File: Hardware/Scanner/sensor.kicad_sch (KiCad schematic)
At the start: 23 parts, among them U1 OPA2376xxD, U4 OPA2376xxD

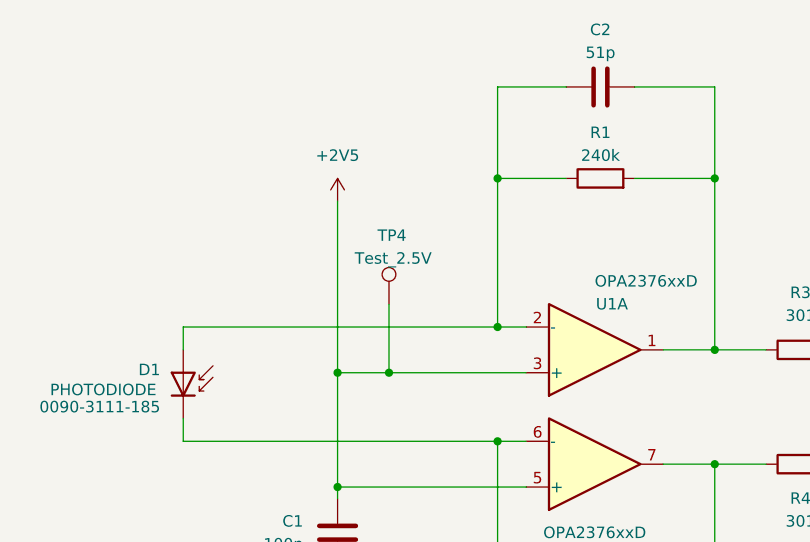
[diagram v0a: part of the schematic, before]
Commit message: Updated LED and crystal descriptions
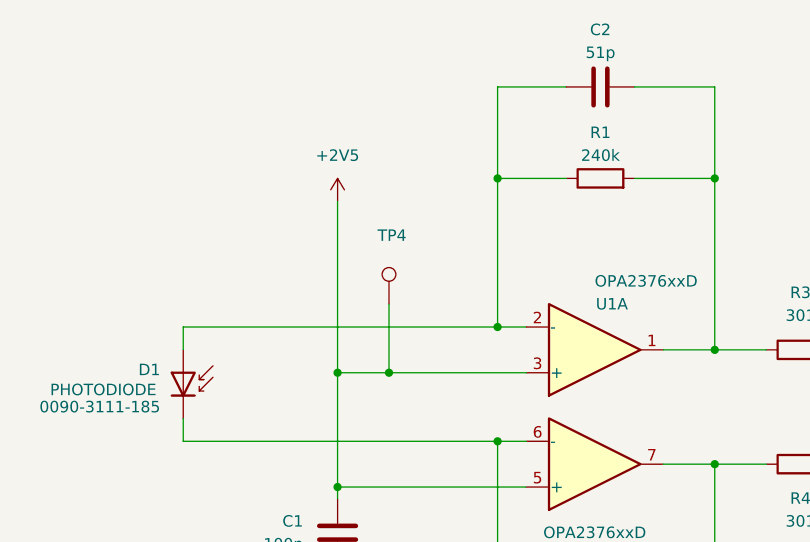
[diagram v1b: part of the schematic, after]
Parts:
- TP4: value Test_2.5V -> (none); footprint TestPoint:TestPoint_Pad_D1.5mm -> (none); now left out of the parts list
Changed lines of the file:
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@@
   )
   (symbol (lib_id "Connector:TestPoint") (at 118.745 46.99 0) (unit 1)
-    (in_bom yes) (on_board yes)
+    (in_bom no) (on_board yes)
     (property "Reference" "TP4" (id 0) (at 117.475 39.37 0)
       (effects (font (size 1.27 1.27)) (justify left))
     )
-    (property "Value" "Test_2.5V" (id 1) (at 114.935 41.91 0)
+    (property "Value" "" (id 1) (at 114.935 41.91 0)
       (effects (font (size 1.27 1.27)) (justify left))
     )
-    (property "Footprint" "TestPoint:TestPoint_Pad_D1.5mm" (id 2) (at 123.825 46.99 0)
+    (property "Footprint" "" (id 2) (at 123.825 46.99 0)
       (effects (font (size 1.27 1.27)) hide)
     )

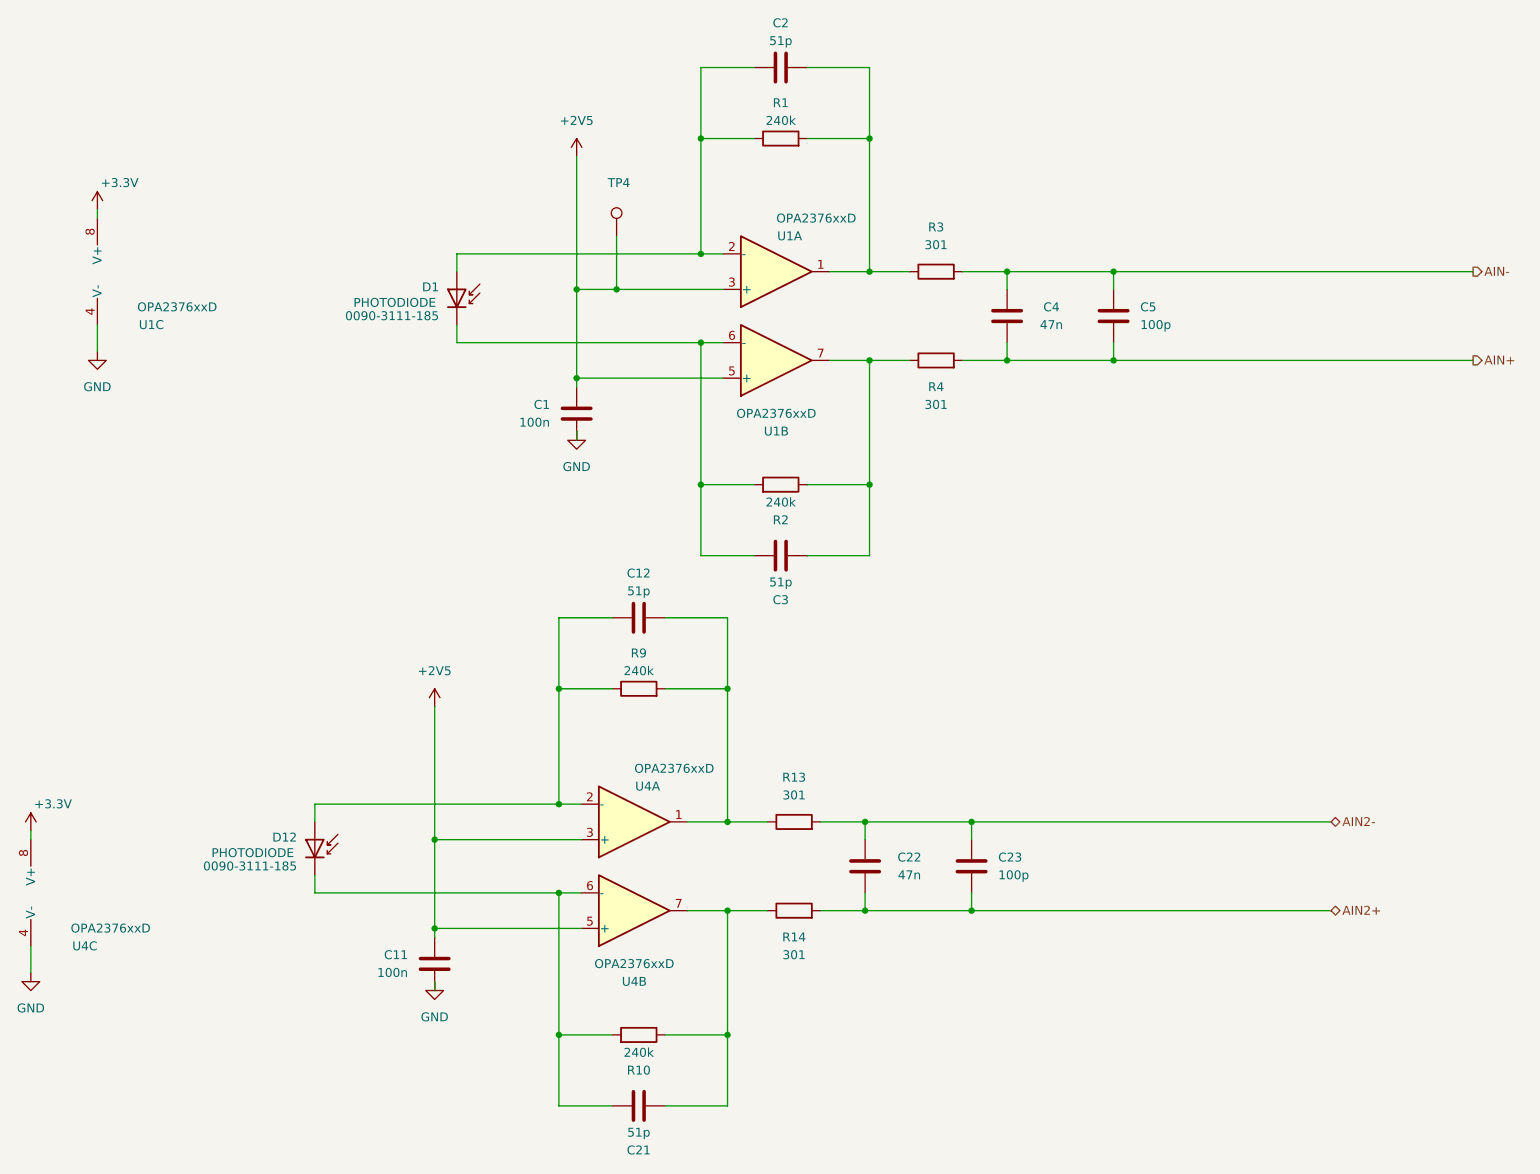
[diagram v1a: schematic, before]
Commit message: Consistency of capacitor values
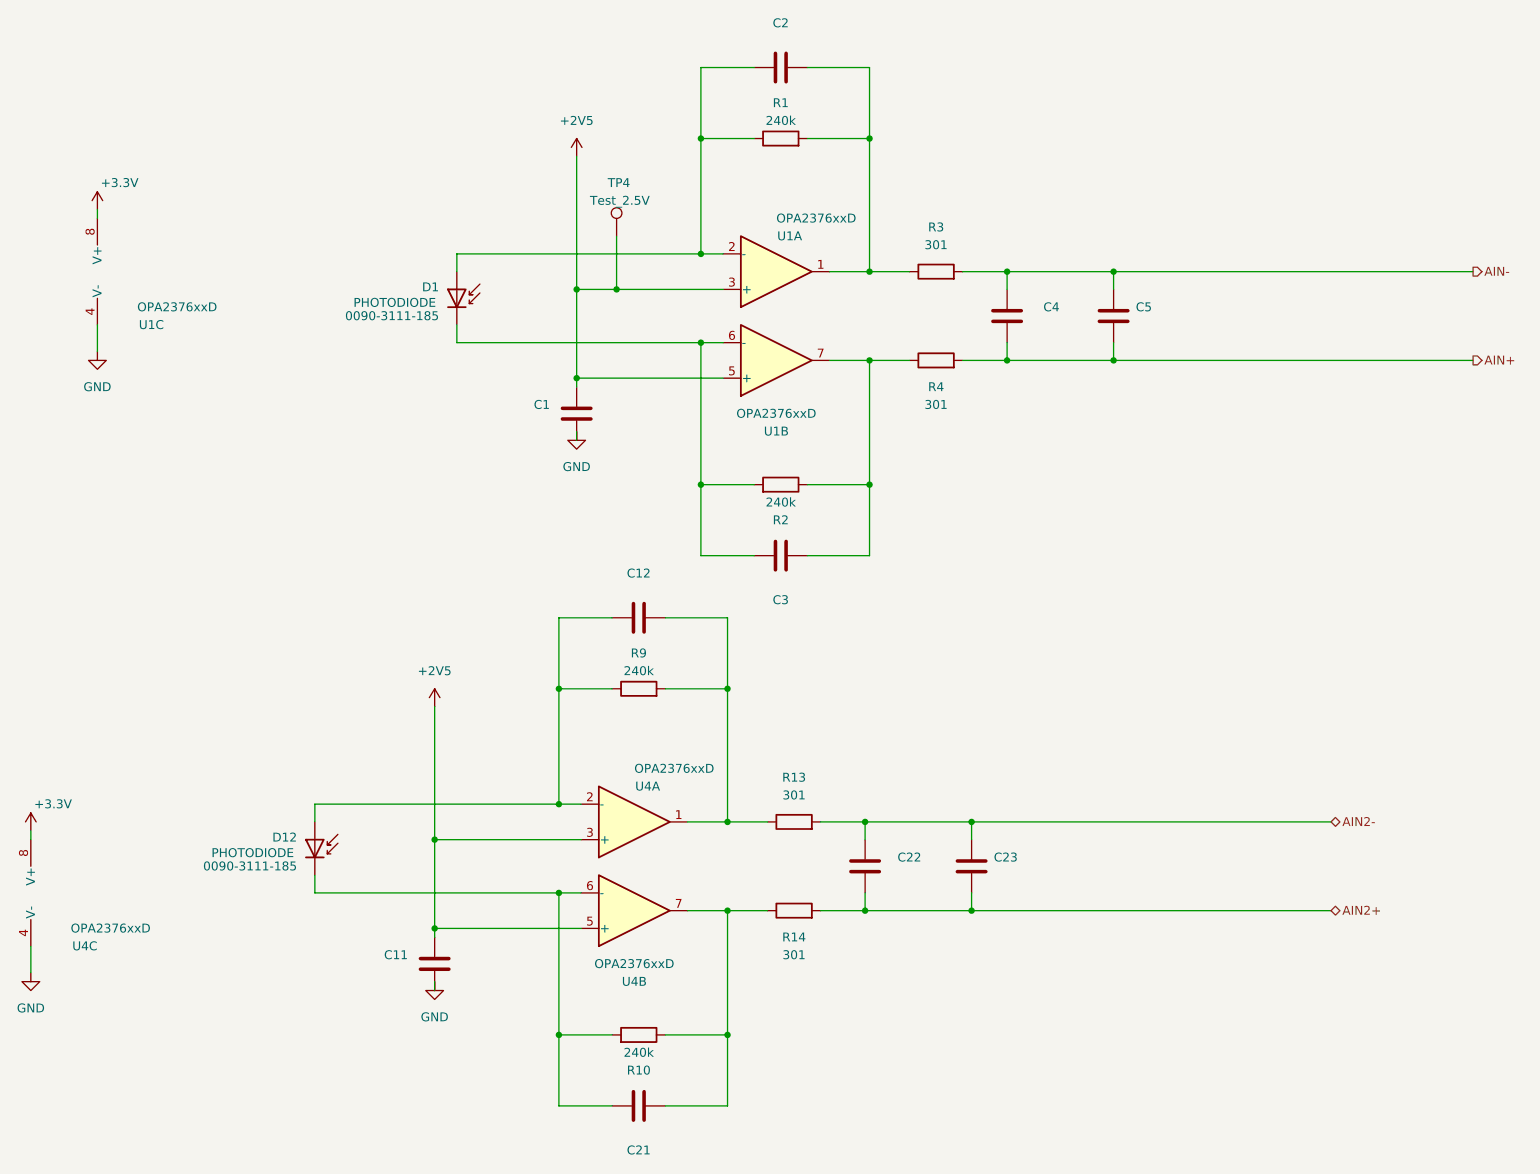
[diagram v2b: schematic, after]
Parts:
- C1, C11: value 100n -> (none)
- C12, C2, C21, C3: value 51p -> (none)
- C22, C4: value 47n -> (none)
- C23, C5: value 100p -> (none)
- TP4: value (none) -> Test_2.5V; footprint (none) -> TestPoint:TestPoint_Pad_D1.5mm
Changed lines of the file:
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@@
       (effects (font (size 1.27 1.27)) (justify right))
     )
-    (property "Value" "100n" (id 1) (at 88.9 152.3999 0)
+    (property "Value" "" (id 1) (at 88.9 152.3999 0)
       (effects (font (size 1.27 1.27)) (justify right))
     )
@@
   (symbol (lib_id "Device:C") (at 189.865 58.42 0) (unit 1)
     (in_bom yes) (on_board yes) (fields_autoplaced)
-    (property "Reference" "C5" (id 0) (at 193.675 57.1499 0)
+    (property "Reference" "C5" (id 0) (at 193.04 57.1499 0)
       (effects (font (size 1.27 1.27)) (justify left))
     )
-    (property "Value" "100p" (id 1) (at 193.675 59.6899 0)
+    (property "Value" "" (id 1) (at 193.04 59.6899 0)
       (effects (font (size 1.27 1.27)) (justify left))
     )
@@
       (effects (font (size 1.27 1.27)) (justify left))
     )
-    (property "Value" "" (id 1) (at 114.935 41.91 0)
+    (property "Value" "Test_2.5V" (id 1) (at 114.935 41.91 0)
       (effects (font (size 1.27 1.27)) (justify left))
     )
-    (property "Footprint" "" (id 2) (at 123.825 46.99 0)
+    (property "Footprint" "TestPoint:TestPoint_Pad_D1.5mm" (id 2) (at 123.825 46.99 0)
       (effects (font (size 1.27 1.27)) hide)
     )
@@
   (symbol (lib_id "Device:C") (at 169.545 137.16 0) (unit 1)
     (in_bom yes) (on_board yes) (fields_autoplaced)
-    (property "Reference" "C23" (id 0) (at 173.355 135.8899 0)
+    (property "Reference" "C23" (id 0) (at 172.72 135.8899 0)
       (effects (font (size 1.27 1.27)) (justify left))
     )
-    (property "Value" "100p" (id 1) (at 173.355 138.4299 0)
+    (property "Value" "" (id 1) (at 172.72 138.4299 0)
       (effects (font (size 1.27 1.27)) (justify left))
     )
@@
     (in_bom yes) (on_board yes)
     (property "Reference" "C12" (id 0) (at 121.92 95.25 90))
-    (property "Value" "51p" (id 1) (at 121.92 97.79 90))
+    (property "Value" "" (id 1) (at 121.92 97.79 90))
     (property "Footprint" "Capacitor_SMD:C_0603_1608Metric_Pad1.08x0.95mm_HandSolder" (id 2) (at 125.73 100.6348 0)
       (effects (font (size 1.27 1.27)) hide)
@@
     (in_bom yes) (on_board yes)
     (property "Reference" "C3" (id 0) (at 142.24 99.06 90))
-    (property "Value" "51p" (id 1) (at 142.24 96.52 90))
+    (property "Value" "" (id 1) (at 142.24 96.52 90))
     (property "Footprint" "Capacitor_SMD:C_0603_1608Metric_Pad1.08x0.95mm_HandSolder" (id 2) (at 146.05 91.7448 0)
       (effects (font (size 1.27 1.27)) hide)
@@
     (in_bom yes) (on_board yes)
     (property "Reference" "C2" (id 0) (at 142.24 16.51 90))
-    (property "Value" "51p" (id 1) (at 142.24 19.05 90))
+    (property "Value" "" (id 1) (at 142.24 19.05 90))
     (property "Footprint" "Capacitor_SMD:C_0603_1608Metric_Pad1.08x0.95mm_HandSolder" (id 2) (at 146.05 21.8948 0)
       (effects (font (size 1.27 1.27)) hide)
@@
     (in_bom yes) (on_board yes)
     (property "Reference" "C4" (id 0) (at 180.975 57.15 0))
-    (property "Value" "47n" (id 1) (at 180.975 59.69 0))
+    (property "Value" "" (id 1) (at 180.975 59.69 0))
     (property "Footprint" "Capacitor_SMD:C_0603_1608Metric_Pad1.08x0.95mm_HandSolder" (id 2) (at 173.6598 54.61 0)
       (effects (font (size 1.27 1.27)) hide)
@@
     (in_bom yes) (on_board yes)
     (property "Reference" "C22" (id 0) (at 160.655 135.89 0))
-    (property "Value" "47n" (id 1) (at 160.655 138.43 0))
+    (property "Value" "" (id 1) (at 160.655 138.43 0))
     (property "Footprint" "Capacitor_SMD:C_0603_1608Metric_Pad1.08x0.95mm_HandSolder" (id 2) (at 153.3398 133.35 0)
       (effects (font (size 1.27 1.27)) hide)
@@
     (in_bom yes) (on_board yes)
     (property "Reference" "C21" (id 0) (at 121.92 177.8 90))
-    (property "Value" "51p" (id 1) (at 121.92 175.26 90))
+    (property "Value" "" (id 1) (at 121.92 175.26 90))
     (property "Footprint" "Capacitor_SMD:C_0603_1608Metric_Pad1.08x0.95mm_HandSolder" (id 2) (at 125.73 170.4848 0)
       (effects (font (size 1.27 1.27)) hide)
@@
       (effects (font (size 1.27 1.27)) (justify right))
     )
-    (property "Value" "100n" (id 1) (at 109.22 73.6599 0)
-      (effects (font (size 1.27 1.27)) (justify right))
-    )
+    (property "Value" "" (id 1) (at 109.22 73.6599 0)
+      (effects (font (size 1.27 1.27)) (justify right))
+    )

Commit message: LAtching circuit for controller board + minors
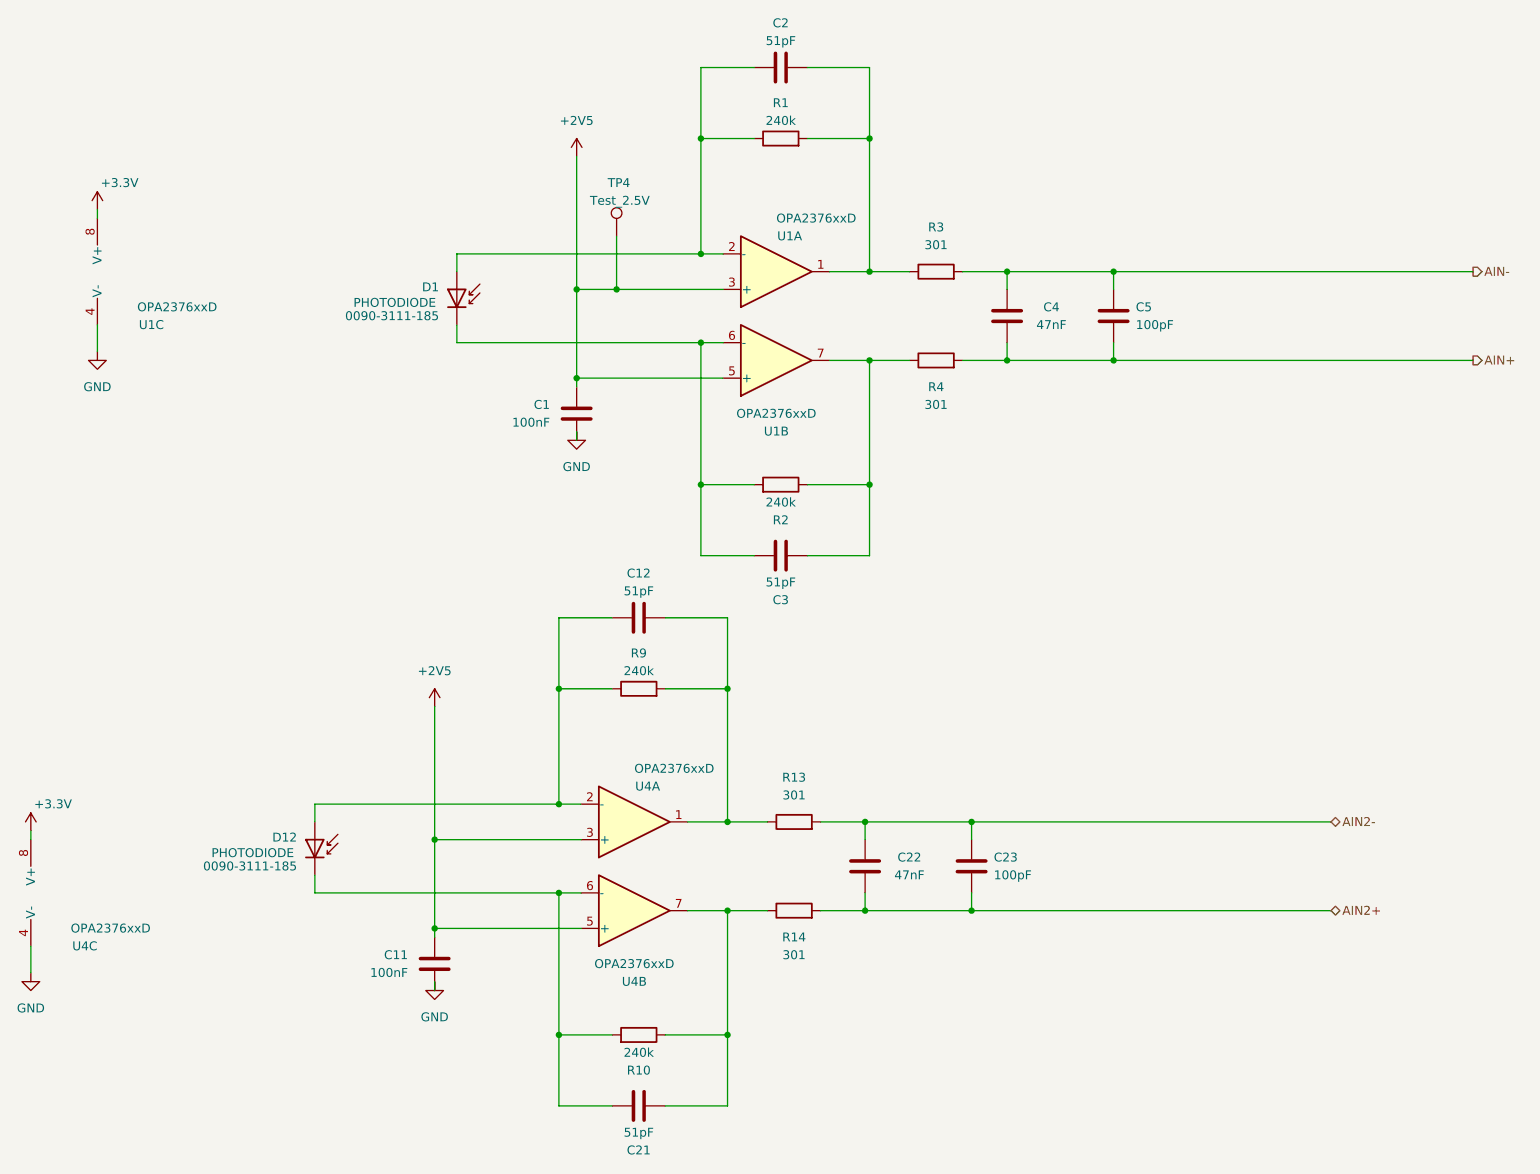
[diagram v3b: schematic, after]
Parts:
- C1, C11: value (none) -> 100nF
- C12, C2, C21, C3: value (none) -> 51pF
- C22, C4: value (none) -> 47nF
- C23, C5: value (none) -> 100pF
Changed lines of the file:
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@@
       (effects (font (size 1.27 1.27)) (justify right))
     )
-    (property "Value" "" (id 1) (at 88.9 152.3999 0)
+    (property "Value" "100nF" (id 1) (at 88.9 152.3999 0)
       (effects (font (size 1.27 1.27)) (justify right))
     )
@@
       (effects (font (size 1.27 1.27)) (justify left))
     )
-    (property "Value" "" (id 1) (at 193.04 59.6899 0)
+    (property "Value" "100pF" (id 1) (at 193.04 59.6899 0)
       (effects (font (size 1.27 1.27)) (justify left))
     )
@@
       (effects (font (size 1.27 1.27)) (justify left))
     )
-    (property "Value" "" (id 1) (at 172.72 138.4299 0)
+    (property "Value" "100pF" (id 1) (at 172.72 138.4299 0)
       (effects (font (size 1.27 1.27)) (justify left))
     )
@@
     (in_bom yes) (on_board yes)
     (property "Reference" "C12" (id 0) (at 121.92 95.25 90))
-    (property "Value" "" (id 1) (at 121.92 97.79 90))
+    (property "Value" "51pF" (id 1) (at 121.92 97.79 90))
     (property "Footprint" "Capacitor_SMD:C_0603_1608Metric_Pad1.08x0.95mm_HandSolder" (id 2) (at 125.73 100.6348 0)
       (effects (font (size 1.27 1.27)) hide)
@@
     (in_bom yes) (on_board yes)
     (property "Reference" "C3" (id 0) (at 142.24 99.06 90))
-    (property "Value" "" (id 1) (at 142.24 96.52 90))
+    (property "Value" "51pF" (id 1) (at 142.24 96.52 90))
     (property "Footprint" "Capacitor_SMD:C_0603_1608Metric_Pad1.08x0.95mm_HandSolder" (id 2) (at 146.05 91.7448 0)
       (effects (font (size 1.27 1.27)) hide)
@@
     (in_bom yes) (on_board yes)
     (property "Reference" "C2" (id 0) (at 142.24 16.51 90))
-    (property "Value" "" (id 1) (at 142.24 19.05 90))
+    (property "Value" "51pF" (id 1) (at 142.24 19.05 90))
     (property "Footprint" "Capacitor_SMD:C_0603_1608Metric_Pad1.08x0.95mm_HandSolder" (id 2) (at 146.05 21.8948 0)
       (effects (font (size 1.27 1.27)) hide)
@@
     (in_bom yes) (on_board yes)
     (property "Reference" "C4" (id 0) (at 180.975 57.15 0))
-    (property "Value" "" (id 1) (at 180.975 59.69 0))
+    (property "Value" "47nF" (id 1) (at 180.975 59.69 0))
     (property "Footprint" "Capacitor_SMD:C_0603_1608Metric_Pad1.08x0.95mm_HandSolder" (id 2) (at 173.6598 54.61 0)
       (effects (font (size 1.27 1.27)) hide)
@@
     (in_bom yes) (on_board yes)
     (property "Reference" "C22" (id 0) (at 160.655 135.89 0))
-    (property "Value" "" (id 1) (at 160.655 138.43 0))
+    (property "Value" "47nF" (id 1) (at 160.655 138.43 0))
     (property "Footprint" "Capacitor_SMD:C_0603_1608Metric_Pad1.08x0.95mm_HandSolder" (id 2) (at 153.3398 133.35 0)
       (effects (font (size 1.27 1.27)) hide)
@@
     (in_bom yes) (on_board yes)
     (property "Reference" "C21" (id 0) (at 121.92 177.8 90))
-    (property "Value" "" (id 1) (at 121.92 175.26 90))
+    (property "Value" "51pF" (id 1) (at 121.92 175.26 90))
     (property "Footprint" "Capacitor_SMD:C_0603_1608Metric_Pad1.08x0.95mm_HandSolder" (id 2) (at 125.73 170.4848 0)
       (effects (font (size 1.27 1.27)) hide)
@@
       (effects (font (size 1.27 1.27)) (justify right))
     )
-    (property "Value" "" (id 1) (at 109.22 73.6599 0)
-      (effects (font (size 1.27 1.27)) (justify right))
-    )
+    (property "Value" "100nF" (id 1) (at 109.22 73.6599 0)
+      (effects (font (size 1.27 1.27)) (justify right))
+    )
